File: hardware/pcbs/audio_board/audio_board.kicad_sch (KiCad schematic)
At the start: 21 parts, among them J1 Header_01x04, J2 MTA100_08, J3 NC3MAH, J4 AudioJack3, J5 NC3MAH, U1 Teensy 4.1

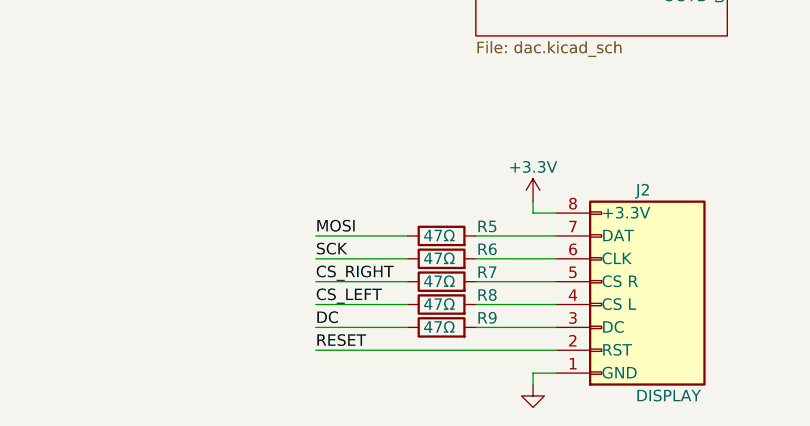
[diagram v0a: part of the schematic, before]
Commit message: Colored netclasses and added lables
- added colored netclasses to easier differentiate analog/digital/power
  lines
- added netnames to previously unnamed nets:
  - PC Mono Input AudioJack3 J9: OUT+T and OUT+R for the nets behind the
    resistors
  - root page: MOSI_R, SCK_R, CS_RIGHT_R, CS_LEFT_R for the nets behind
    the resistors so that the SPI lines can be colored accordingly
- use slightly different colors on PCB to not get blinded when looking
  at it

No functional changes, only cosmetics and net lables.
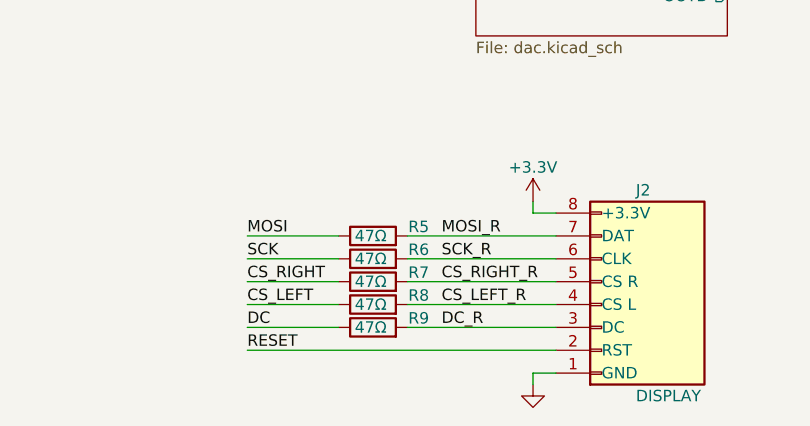
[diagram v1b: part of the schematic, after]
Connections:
- net DC_R: now reaches J2.3 (Pin_3), R9.2
- net CS_LEFT_R: now reaches J2.4 (Pin_4), R8.2
- net CS_RIGHT_R: now reaches J2.5 (Pin_5), R7.2
- net SCK_R: now reaches J2.6 (Pin_6), R6.2
- net MOSI_R: now reaches J2.7 (Pin_7), R5.2
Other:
- moved on the sheet: R5, R6, R7, R8, R9
